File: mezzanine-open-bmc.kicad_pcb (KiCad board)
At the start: 2 copper layers, 85 x 54.1 mm, 51 parts, among them P1 CONN_02X20, P2 CONN_02X20, Q1 S8050, Q2 S8050, SW1 PWR, SW2 RST, U1 FT230XS, U2 PMIC-CJT1117-3.3(SOT223), U4 PCA9306, U5 M24C16-WMN6P

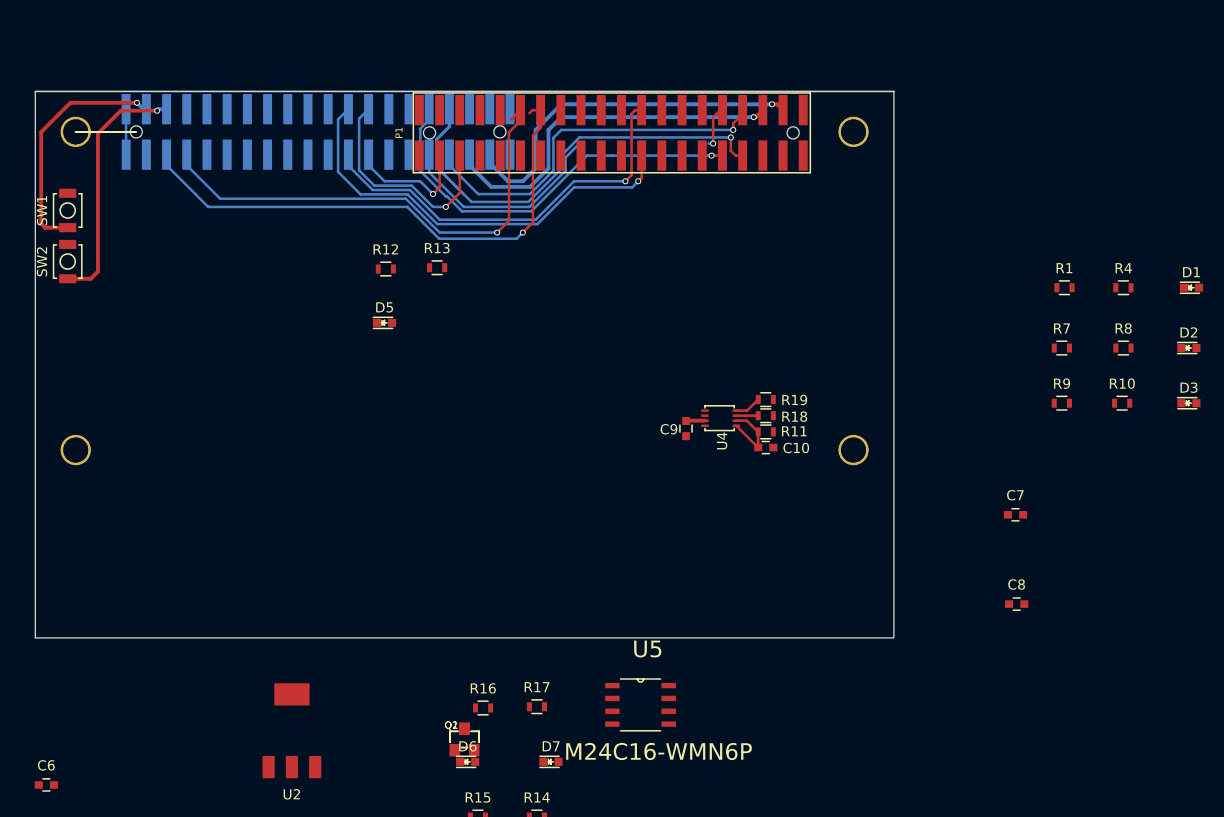
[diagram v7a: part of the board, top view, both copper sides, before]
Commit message: Wire Up BB LED (1.8v)
The wiring for the LED components of 1.8 have been connnected up in a neat little
bundle which can be placed on the board.

Signed-off-by: Sophie Haynes <sophie.haynes@linaro.org>
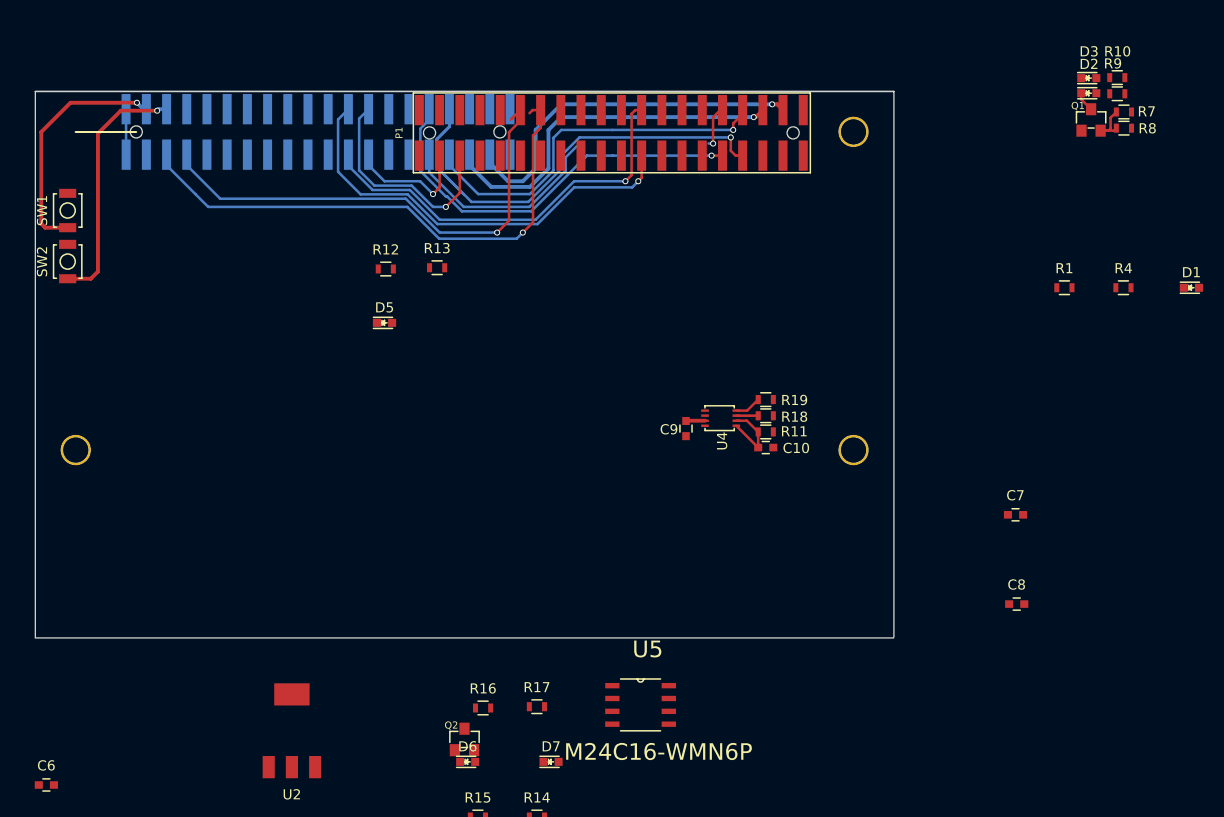
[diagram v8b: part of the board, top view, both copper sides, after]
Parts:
- removed the REF** at (104.0, 104.0)
- moved Q1 87.2 mm to (204.5, 102.8)
- moved D3 33.7 mm to (204.3, 98.7)
- moved R10 32.2 mm to (207.1, 98.6), turned to 180 degrees
- moved R9 31.1 mm to (207.1, 100.2), turned to 180 degrees
- moved D2 27.1 mm to (204.3, 100.2)
- moved R7 24.2 mm to (207.8, 102.0)
- moved R8 21.8 mm to (207.8, 103.6)
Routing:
- net Net-(Q1-Pad2): track 0.00 -> 4.60 mm
- net Net-(D2-Pad1): track 0.00 -> 1.99 mm
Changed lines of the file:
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@@
   (general
     (links 119)
-    (no_connects 88)
+    (no_connects 86)
     (area 99.924599 99.949999 185.049493 154.151601)
     (thickness 1.6)
     (drawings 13)
-    (tracks 197)
+    (tracks 205)
     (zones 0)
-    (modules 51)
+    (modules 50)
     (nets 88)
   )
@@
     (pad 1 thru_hole circle (at 0 0) (size 3 3) (drill 2.5) (layers *.Cu *.Mask))
   )
-  (module Sensors:Hole_2.5MM (layer F.Cu)
-    (at 104 104)
-    (fp_text reference REF** (at 0 0.5) (layer F.SilkS) hide
-      (effects (font (size 1 1) (thickness 0.15)))
-    )
-    (fp_text value Hole_2.5MM (at 0 -0.5) (layer F.Fab) hide
-      (effects (font (size 1 1) (thickness 0.15)))
-    )
-    (pad 1 thru_hole circle (at 0 0) (size 3 3) (drill 2.5) (layers *.Cu *.Mask))
-  )
   (module Capacitors_SMD:C_0603 (layer F.Cu)
     (at 53.1622 100.6348)
@@
   )
   (module LEDs:LED_0603 (layer F.Cu)
-    (at 214.1984 125.4)
+    (at 204.2922 100.1776)
     (descr "LED 0603 smd package")
     (tags "LED led 0603 SMD smd SMT smt smdled SMDLED smtled SMTLED")
     (attr smd)
-    (fp_text reference D2 (at 0 -1.5) (layer F.SilkS)
-      (effects (font (size 1 1) (thickness 0.15)))
-    )
-    (fp_text value Led_Small (at 0 1.5) (layer F.Fab)
+    (fp_text reference D2 (at 0.0254 -2.8702) (layer F.SilkS)
+      (effects (font (size 1 1) (thickness 0.15)))
+    )
+    (fp_text value Led_Small (at 0 1.5) (layer F.Fab) hide
       (effects (font (size 1 1) (thickness 0.15)))
     )
@@
   )
   (module LEDs:LED_0603 (layer F.Cu)
-    (at 214.1984 130.861)
+    (at 204.2922 98.679)
     (descr "LED 0603 smd package")
     (tags "LED led 0603 SMD smd SMT smt smdled SMDLED smtled SMTLED")
     (attr smd)
-    (fp_text reference D3 (at 0 -1.5) (layer F.SilkS)
-      (effects (font (size 1 1) (thickness 0.15)))
-    )
-    (fp_text value Led_Small (at 0 1.5) (layer F.Fab)
+    (fp_text reference D3 (at 0.0254 -2.6162) (layer F.SilkS)
+      (effects (font (size 1 1) (thickness 0.15)))
+    )
+    (fp_text value Led_Small (at 0 1.5) (layer F.Fab) hide
       (effects (font (size 1 1) (thickness 0.15)))
     )
@@
   )
   (module Resistors_SMD:R_0603 (layer F.Cu)
-    (at 201.6254 125.4)
+    (at 207.772 102.0318)
     (descr "Resistor SMD 0603, reflow soldering, Vishay (see dcrcw.pdf)")
     (tags "resistor 0603")
     (attr smd)
-    (fp_text reference R7 (at 0 -1.9) (layer F.SilkS)
-      (effects (font (size 1 1) (thickness 0.15)))
-    )
-    (fp_text value 1k (at 0 1.9) (layer F.Fab)
+    (fp_text reference R7 (at 2.2606 -0.0254) (layer F.SilkS)
+      (effects (font (size 1 1) (thickness 0.15)))
+    )
+    (fp_text value 1k (at 0 1.9) (layer F.Fab) hide
       (effects (font (size 1 1) (thickness 0.15)))
     )
@@
   )
   (module Resistors_SMD:R_0603 (layer F.Cu)
-    (at 207.7214 125.4)
+    (at 207.772 103.632)
     (descr "Resistor SMD 0603, reflow soldering, Vishay (see dcrcw.pdf)")
     (tags "resistor 0603")
     (attr smd)
-    (fp_text reference R8 (at 0 -1.9) (layer F.SilkS)
-      (effects (font (size 1 1) (thickness 0.15)))
-    )
-    (fp_text value 10k (at 0 1.9) (layer F.Fab)
+    (fp_text reference R8 (at 2.3368 0.0508) (layer F.SilkS)
+      (effects (font (size 1 1) (thickness 0.15)))
+    )
+    (fp_text value 10k (at 0 1.9) (layer F.Fab) hide
       (effects (font (size 1 1) (thickness 0.15)))
     )
@@
   )
   (module Resistors_SMD:R_0603 (layer F.Cu)
-    (at 201.6254 130.861)
+    (at 207.1116 100.2284 180)
     (descr "Resistor SMD 0603, reflow soldering, Vishay (see dcrcw.pdf)")
     (tags "resistor 0603")
     (attr smd)
-    (fp_text reference R9 (at 0 -1.9) (layer F.SilkS)
-      (effects (font (size 1 1) (thickness 0.15)))
-    )
-    (fp_text value 390R (at 0 1.9) (layer F.Fab)
+    (fp_text reference R9 (at 0.4318 2.9718 180) (layer F.SilkS)
+      (effects (font (size 1 1) (thickness 0.15)))
+    )
+    (fp_text value 390R (at 0 1.9 180) (layer F.Fab) hide
       (effects (font (size 1 1) (thickness 0.15)))
     )
@@
     (fp_line (start 0.5 0.675) (end -0.5 0.675) (layer F.SilkS) (width 0.15))
     (fp_line (start -0.5 -0.675) (end 0.5 -0.675) (layer F.SilkS) (width 0.15))
-    (pad 1 smd rect (at -0.75 0) (size 0.5 0.9) (layers F.Cu F.Paste F.Mask)
+    (pad 1 smd rect (at -0.75 0 180) (size 0.5 0.9) (layers F.Cu F.Paste F.Mask)
       (net 1 +1V8))
-    (pad 2 smd rect (at 0.75 0) (size 0.5 0.9) (layers F.Cu F.Paste F.Mask)
+    (pad 2 smd rect (at 0.75 0 180) (size 0.5 0.9) (layers F.Cu F.Paste F.Mask)
       (net 39 "Net-(D2-Pad2)"))
     (model Resistors_SMD.3dshapes/R_0603.wrl
@@
   )
   (module Resistors_SMD:R_0603 (layer F.Cu)
-    (at 207.5944 130.861)
+    (at 207.1116 98.6282 180)
     (descr "Resistor SMD 0603, reflow soldering, Vishay (see dcrcw.pdf)")
     (tags "resistor 0603")
     (attr smd)
-    (fp_text reference R10 (at 0 -1.9) (layer F.SilkS)
-      (effects (font (size 1 1) (thickness 0.15)))
-    )
-    (fp_text value 620R (at 0 1.9) (layer F.Fab)
+    (fp_text reference R10 (at -0.0254 2.5654 180) (layer F.SilkS)
+      (effects (font (size 1 1) (thickness 0.15)))
+    )
+    (fp_text value 620R (at 0 1.9 180) (layer F.Fab) hide
       (effects (font (size 1 1) (thickness 0.15)))
     )
@@
     (fp_line (start 0.5 0.675) (end -0.5 0.675) (layer F.SilkS) (width 0.15))
     (fp_line (start -0.5 -0.675) (end 0.5 -0.675) (layer F.SilkS) (width 0.15))
-    (pad 1 smd rect (at -0.75 0) (size 0.5 0.9) (layers F.Cu F.Paste F.Mask)
+    (pad 1 smd rect (at -0.75 0 180) (size 0.5 0.9) (layers F.Cu F.Paste F.Mask)
       (net 1 +1V8))
-    (pad 2 smd rect (at 0.75 0) (size 0.5 0.9) (layers F.Cu F.Paste F.Mask)
+    (pad 2 smd rect (at 0.75 0 180) (size 0.5 0.9) (layers F.Cu F.Paste F.Mask)
       (net 41 "Net-(D3-Pad2)"))
     (model Resistors_SMD.3dshapes/R_0603.wrl
@@
   )
   (module 96boards:SOT-23_Seeed (layer F.Cu)
-    (at 142.487046 164.151601)
+    (at 204.5208 102.8192)
     (descr "SOT-23, Standard")
     (tags SOT-23)
@@
   (segment (start 171.5516 133.7056) (end 170.442 132.596) (width 0.254) (layer F.Cu) (net 36))
   (segment (start 170.442 132.596) (end 169.3938 132.596) (width 0.254) (layer F.Cu) (net 36))
+  (segment (start 203.5429 100.1776) (end 203.5429 100.7813) (width 0.254) (layer F.Cu) (net 40))
+  (segment (start 203.5429 100.7813) (end 204.5208 101.7592) (width 0.254) (layer F.Cu) (net 40))
   (segment (start 138.1 108.89) (end 134.5728 108.89) (width 0.254) (layer B.Cu) (net 46))
   (segment (start 134.5728 108.89) (end 132.9916 107.3088) (width 0.254) (layer B.Cu) (net 46))
@@
   (segment (start 55.9978 98.1583) (end 54.8393 98.1583) (width 0.254) (layer F.Cu) (net 74))
   (segment (start 54.8393 98.1583) (end 53.9122 99.0854) (width 0.254) (layer F.Cu) (net 74))
+  (segment (start 205.4708 103.8792) (end 206.2548 103.8792) (width 0.254) (layer F.Cu) (net 75))
+  (segment (start 206.4512 102.6026) (end 207.022 102.0318) (width 0.254) (layer F.Cu) (net 75))
+  (segment (start 206.4512 103.6828) (end 206.4512 102.6026) (width 0.254) (layer F.Cu) (net 75))
+  (segment (start 206.2548 103.8792) (end 206.4512 103.6828) (width 0.254) (layer F.Cu) (net 75))
+  (segment (start 205.4708 103.8792) (end 206.7748 103.8792) (width 0.254) (layer F.Cu) (net 75))
+  (segment (start 206.7748 103.8792) (end 207.022 103.632) (width 0.254) (layer F.Cu) (net 75))
   (segment (start 108.9816 101.7538) (end 108.9816 106.2438) (width 0.254) (layer B.Cu) (net 82))
   (segment (start 108.9816 106.2438) (end 108.9916 106.2538) (width 0.254) (layer B.Cu) (net 82))
